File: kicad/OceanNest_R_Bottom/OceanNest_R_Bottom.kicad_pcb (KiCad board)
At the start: 2 copper layers, 103.5 x 88.7 mm, 4 parts

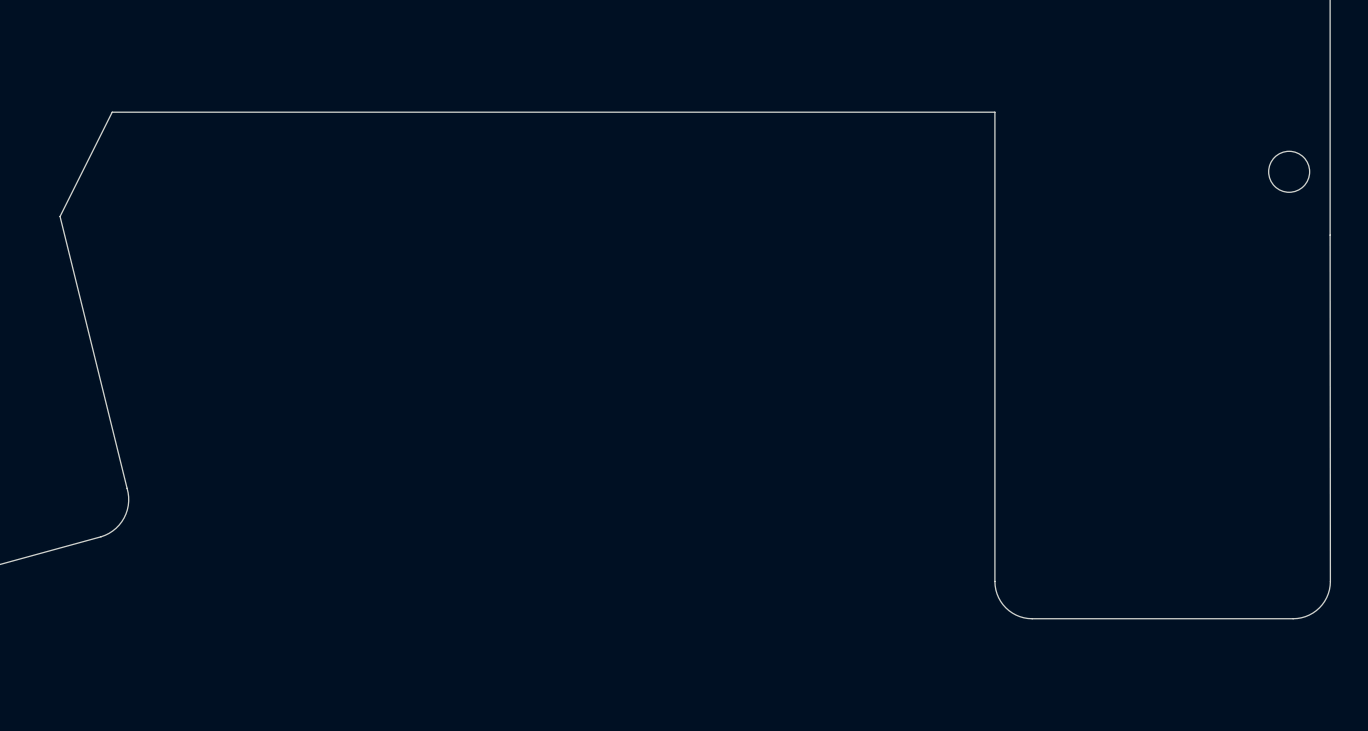
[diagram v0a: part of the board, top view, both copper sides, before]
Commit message: fix: update filenames and step files in OceanNest project for consistency and clarity
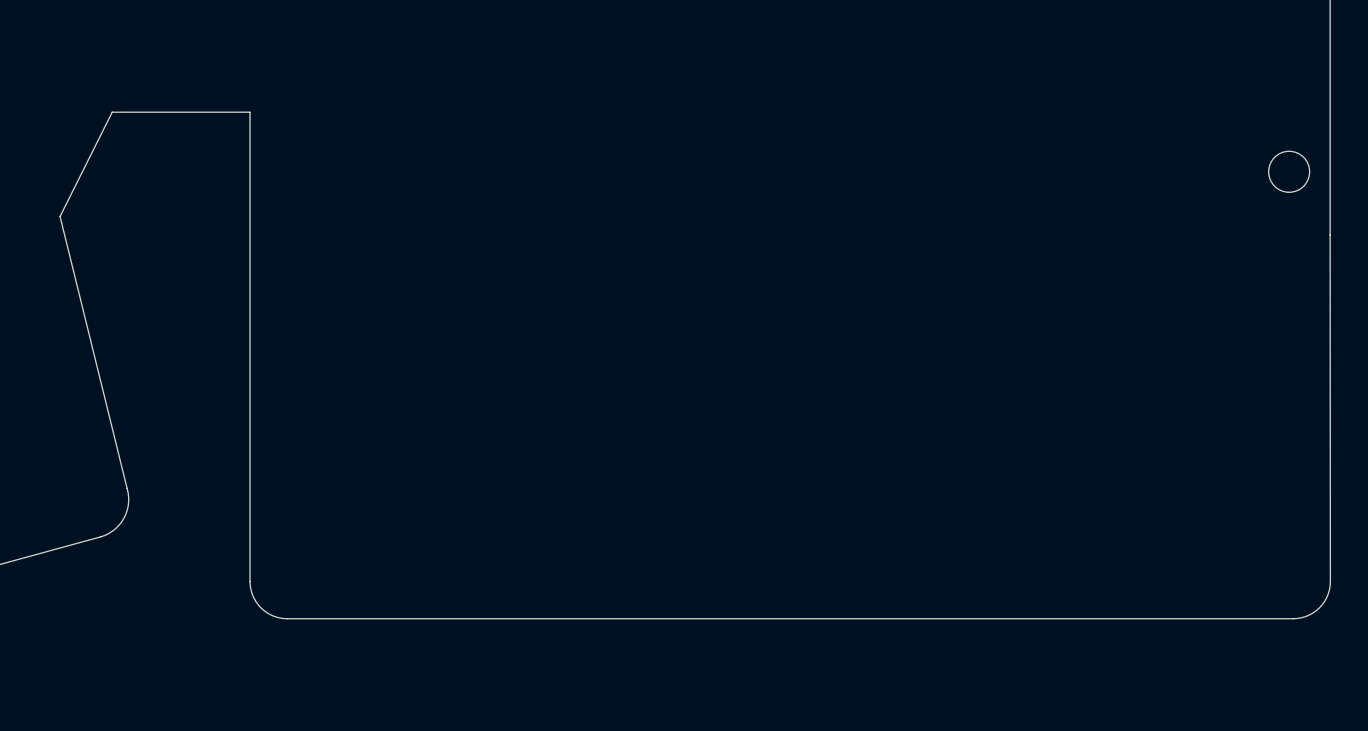
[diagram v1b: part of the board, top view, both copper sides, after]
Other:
- outline, holes or cut-outs redrawn
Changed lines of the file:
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@@
 	)
 	(gr_arc
-		(start 162 143.2)
-		(mid 160.585786 142.614214)
-		(end 160 141.2)
+		(start 122 143.2)
+		(mid 120.585786 142.614214)
+		(end 120 141.2)
 		(stroke
 			(width 0.05)
@@
 	)
 	(gr_line
-		(start 160 116)
-		(end 160 141.2)
+		(start 120 116)
+		(end 120 141.2)
 		(stroke
 			(width 0.05)
@@
 	(gr_line
 		(start 112.6 116)
-		(end 160 116)
+		(end 120 116)
 		(stroke
 			(width 0.05)
@@
 	)
 	(gr_line
-		(start 162 143.2)
+		(start 122 143.2)
 		(end 176.014214 143.2)
 		(stroke

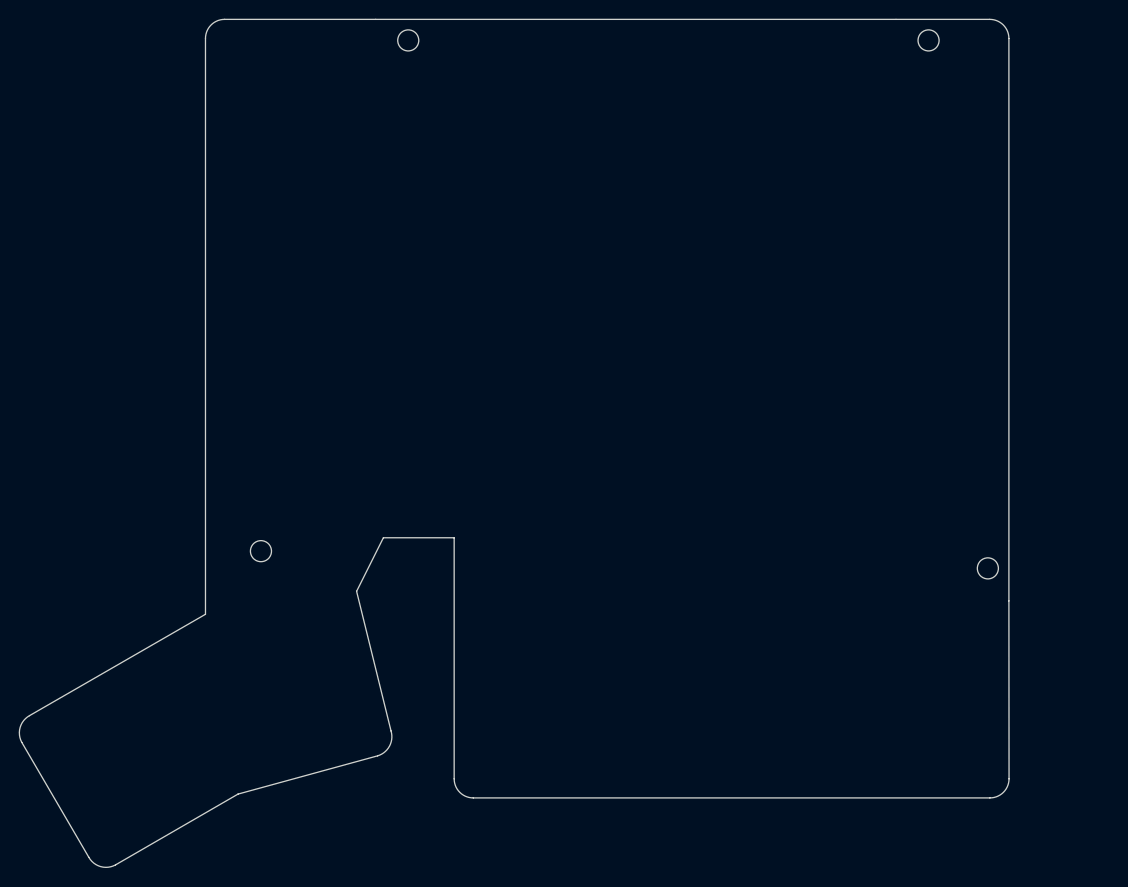
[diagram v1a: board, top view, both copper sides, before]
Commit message: feat: add new OceanNest_L and OceanNest_R PCB and project files for enhanced design capabilities
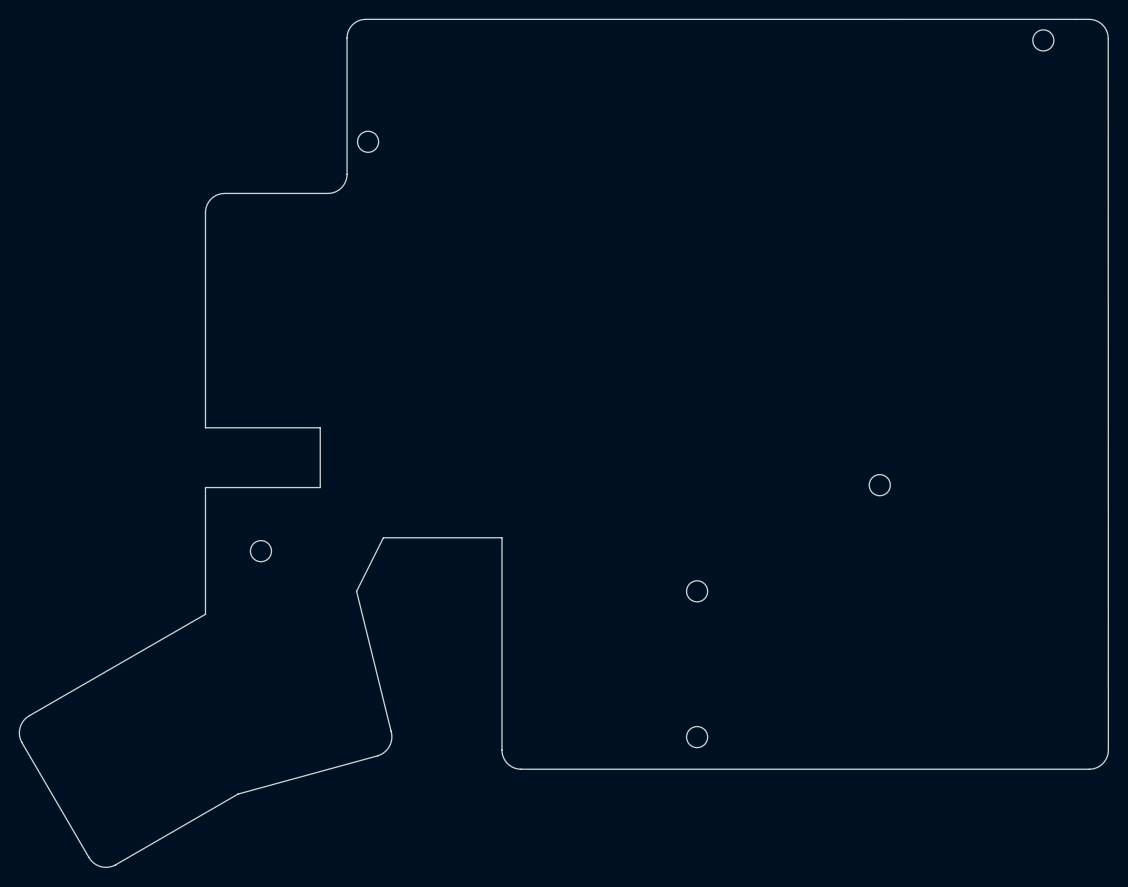
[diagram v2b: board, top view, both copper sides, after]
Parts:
- removed Ref** (x3): Val**, isw-kbd:M2_ScrewHole
- added hole2: Val**, kbd_Hole:m2_Screw_Hole, F.Cu at (145.4, 136.8)
- added hole2: Val**, kbd_Hole:m2_Screw_Hole, F.Cu at (164.5, 110.5)
- added hole2: Val**, kbd_Hole:m2_Screw_Hole, F.Cu at (145.4, 121.6)
- added hole2: Val**, kbd_Hole:m2_Screw_Hole, F.Cu at (181.6, 64.0)
- added hole2: Val**, kbd_Hole:m2_Screw_Hole, F.Cu at (111.0, 74.6)
- hole1: renamed from Ref**; footprint isw-kbd:M2_ScrewHole -> kbd_Hole:m2_Screw_Hole
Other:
- board size 103.5 x 88.7 mm -> 113.9 x 88.7 mm
